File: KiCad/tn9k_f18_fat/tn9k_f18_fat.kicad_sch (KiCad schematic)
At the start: 9 parts, among them J1 Conn_01x20, J2 Conn_01x20, J3 Conn_01x24, J4 Conn_01x24, J5 Conn_02x04_Counter_Clockwise, J6 Conn_02x08_Odd_Even, U1 SN74LVC245, U2 SN74LVC245, U3 SN74LVC245

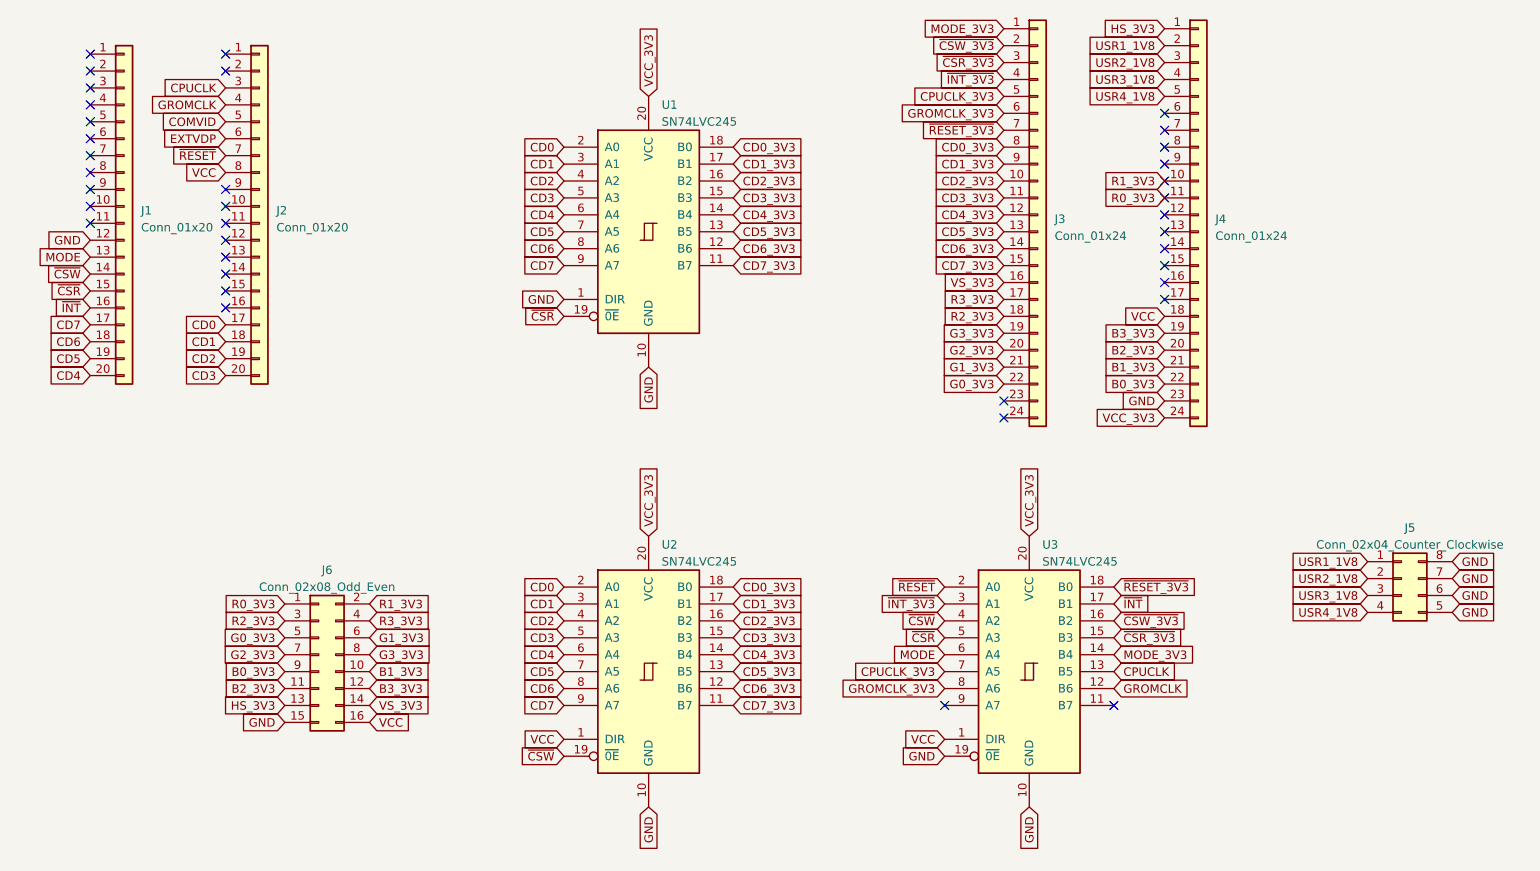
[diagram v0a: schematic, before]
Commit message: update FAT board for the diode
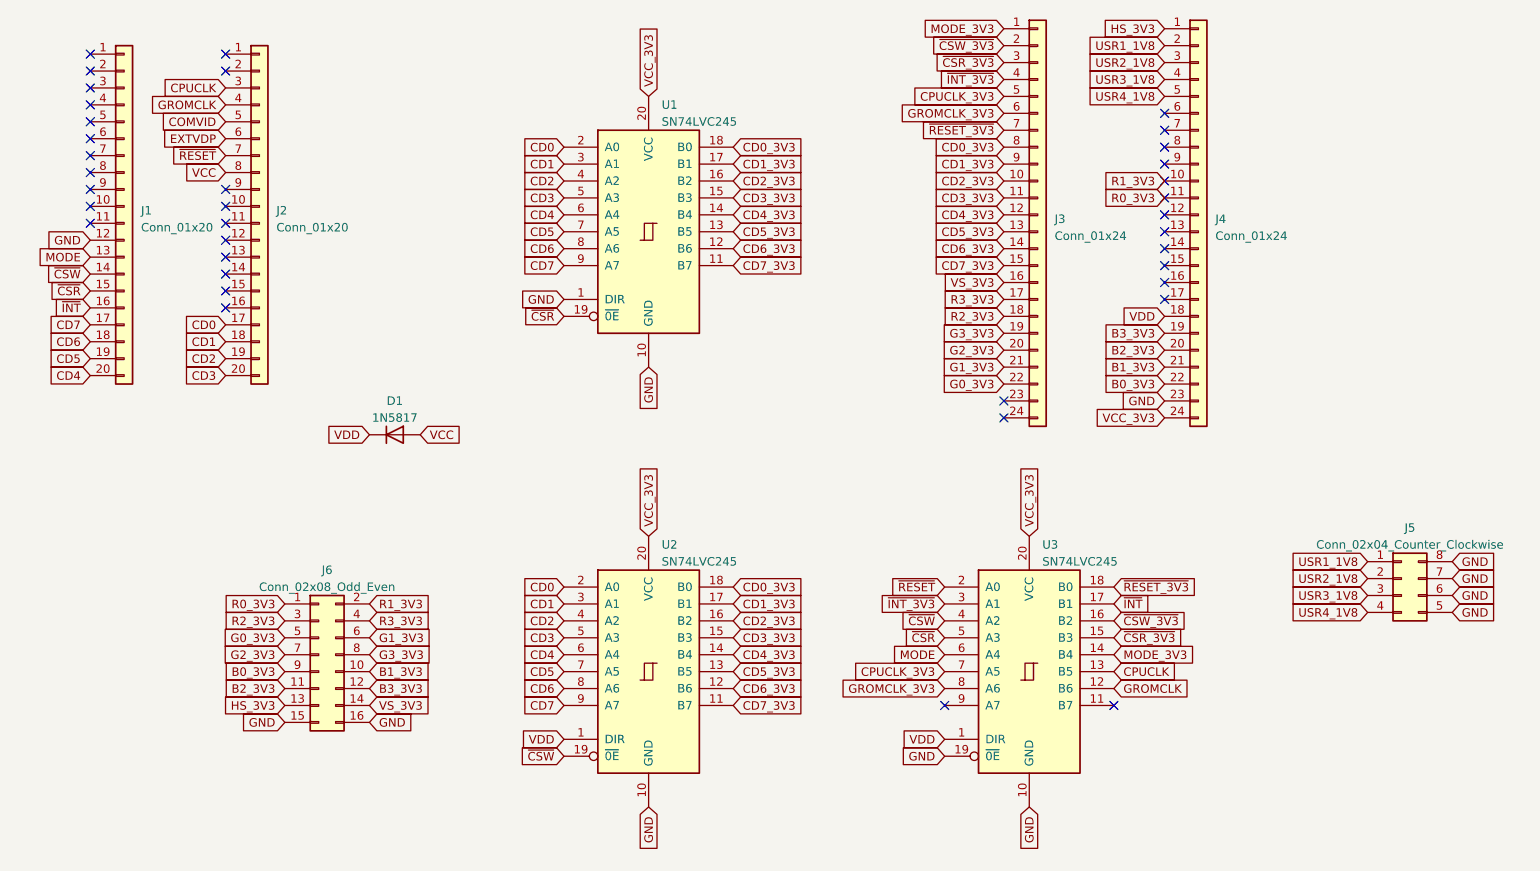
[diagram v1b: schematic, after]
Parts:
- added D1: 1N5817, Diode_THT:D_DO-41_SOD81_P10.16mm_Horizontal, symbol Diode:1N4001
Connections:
- net GND: now also J6.16 (Pin_16)
- net VCC: now also D1.2 (A); no longer J4.18 (Pin_18), J6.16 (Pin_16), U2.1 (DIR), U3.1 (DIR)
- new net VDD: D1.1 (K), J4.18 (Pin_18), U2.1 (DIR), U3.1 (DIR)
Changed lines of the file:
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@@
+    )
+  )
+  (global_label "VCC" (shape input) (at 114.3 81.28 0) (fields_autoplaced)
+    (effects (font (size 1.27 1.27)) (justify left))
+    (property "Intersheetrefs" "${INTERSHEET_REFS}" (at 120.8344 81.28 0)
+      (effects (font (size 1.27 1.27)) (justify left) hide)
     )
   )
@@
     )
   )
-  (global_label "VCC" (shape input) (at 226.06 63.5 180) (fields_autoplaced)
+  (global_label "VDD" (shape input) (at 226.06 63.5 180) (fields_autoplaced)
     (effects (font (size 1.27 1.27)) (justify right))
     (property "Intersheetrefs" "${INTERSHEET_REFS}" (at 219.5256 63.5 0)
@@
     )
   )
+  (global_label "VDD" (shape input) (at 106.68 81.28 180) (fields_autoplaced)
+    (effects (font (size 1.27 1.27)) (justify right))
+    (property "Intersheetrefs" "${INTERSHEET_REFS}" (at 100.1456 81.28 0)
+      (effects (font (size 1.27 1.27)) (justify right) hide)
+    )
+  )
   (global_label "~{CSW}" (shape input) (at 135.89 129.54 180) (fields_autoplaced)
     (effects (font (size 1.27 1.27)) (justify right))
@@
     )
   )
-  (global_label "VCC" (shape input) (at 193.04 127 180) (fields_autoplaced)
+  (global_label "VDD" (shape input) (at 193.04 127 180) (fields_autoplaced)
     (effects (font (size 1.27 1.27)) (justify right))
     (property "Intersheetrefs" "${INTERSHEET_REFS}" (at 186.5056 127 0)
@@
     )
   )
-  (global_label "VCC" (shape input) (at 135.89 127 180) (fields_autoplaced)
+  (global_label "VDD" (shape input) (at 135.89 127 180) (fields_autoplaced)
     (effects (font (size 1.27 1.27)) (justify right))
     (property "Intersheetrefs" "${INTERSHEET_REFS}" (at 129.3556 127 0)
@@
     )
   )
+  (global_label "GND" (shape input) (at 106.68 124.46 0) (fields_autoplaced)
+    (effects (font (size 1.27 1.27)) (justify left))
+    (property "Intersheetrefs" "${INTERSHEET_REFS}" (at 113.4563 124.46 0)
+      (effects (font (size 1.27 1.27)) (justify left) hide)
+    )
+  )
   (global_label "G3_3V3" (shape input) (at 201.93 66.04 180) (fields_autoplaced)
     (effects (font (size 1.27 1.27)) (justify right))
     (property "Intersheetrefs" "${INTERSHEET_REFS}" (at 192.0695 66.04 0)
       (effects (font (size 1.27 1.27)) (justify right) hide)
-    )
-  )
-  (global_label "VCC" (shape input) (at 106.68 124.46 0) (fields_autoplaced)
-    (effects (font (size 1.27 1.27)) (justify left))
-    (property "Intersheetrefs" "${INTERSHEET_REFS}" (at 113.2144 124.46 0)
-      (effects (font (size 1.27 1.27)) (justify left) hide)
     )
   )
@@
     (pin "9")
     (instances
-      (project "tn9k_f18_cross"
+      (project "tn9k_f18_fat"
         (path "/e3c6ad0b-efa5-4827-958c-c20bf8519fa1"
           (reference "J1") (unit 1)
@@
     (pin "9")
     (instances
-      (project "tn9k_f18_cross"
+      (project "tn9k_f18_fat"
         (path "/e3c6ad0b-efa5-4827-958c-c20bf8519fa1"
           (reference "U3") (unit 1)
@@
     (pin "8")
     (instances
-      (project "tn9k_f18_cross"
+      (project "tn9k_f18_fat"
         (path "/e3c6ad0b-efa5-4827-958c-c20bf8519fa1"
           (reference "J5") (unit 1)
@@
     (pin "9")
     (instances
-      (project "tn9k_f18_cross"
+      (project "tn9k_f18_fat"
         (path "/e3c6ad0b-efa5-4827-958c-c20bf8519fa1"
           (reference "J3") (unit 1)
@@
     (pin "9")
     (instances
-      (project "tn9k_f18_cross"
+      (project "tn9k_f18_fat"
         (path "/e3c6ad0b-efa5-4827-958c-c20bf8519fa1"
           (reference "J6") (unit 1)
@@
     (pin "9")
     (instances
-      (project "tn9k_f18_cross"
+      (project "tn9k_f18_fat"
         (path "/e3c6ad0b-efa5-4827-958c-c20bf8519fa1"
           (reference "J2") (unit 1)
@@
     (pin "9")
     (instances
-      (project "tn9k_f18_cross"
+      (project "tn9k_f18_fat"
         (path "/e3c6ad0b-efa5-4827-958c-c20bf8519fa1"
           (reference "U1") (unit 1)
+        )
+      )
+    )
+  )
+  (symbol (lib_id "Diode:1N4001") (at 110.49 81.28 0) (unit 1)
+    (in_bom yes) (on_board yes) (dnp no) (fields_autoplaced)
+    (property "Reference" "D1" (at 110.49 76.2 0)
+      (effects (font (size 1.27 1.27)))
+    )
+    (property "Value" "1N5817" (at 110.49 78.74 0)
+      (effects (font (size 1.27 1.27)))
+    )
+    (property "Footprint" "Diode_THT:D_DO-41_SOD81_P10.16mm_Horizontal" (at 110.49 81.28 0)
+      (effects (font (size 1.27 1.27)) hide)
+    )
+    (property "Datasheet" "http://www.vishay.com/docs/88503/1n4001.pdf" (at 110.49 81.28 0)
+      (effects (font (size 1.27 1.27)) hide)
+    )
+    (property "Sim.Device" "D" (at 110.49 81.28 0)
+      (effects (font (size 1.27 1.27)) hide)
+    )
+    (property "Sim.Pins" "1=K 2=A" (at 110.49 81.28 0)
+      (effects (font (size 1.27 1.27)) hide)
+    )
+    (pin "1")
+    (pin "2")
+    (instances
+      (project "tn9k_f18_fat"
+        (path "/e3c6ad0b-efa5-4827-958c-c20bf8519fa1"
+          (reference "D1") (unit 1)
         )
       )
@@
     (pin "9")
     (instances
-      (project "tn9k_f18_cross"
+      (project "tn9k_f18_fat"
         (path "/e3c6ad0b-efa5-4827-958c-c20bf8519fa1"
           (reference "J4") (unit 1)
@@
     (pin "9")
     (instances
-      (project "tn9k_f18_cross"
+      (project "tn9k_f18_fat"
         (path "/e3c6ad0b-efa5-4827-958c-c20bf8519fa1"
           (reference "U2") (unit 1)
